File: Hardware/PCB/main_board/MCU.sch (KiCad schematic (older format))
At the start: 2 parts, among them J1 SWD, U2 NUCLEO-F446RE

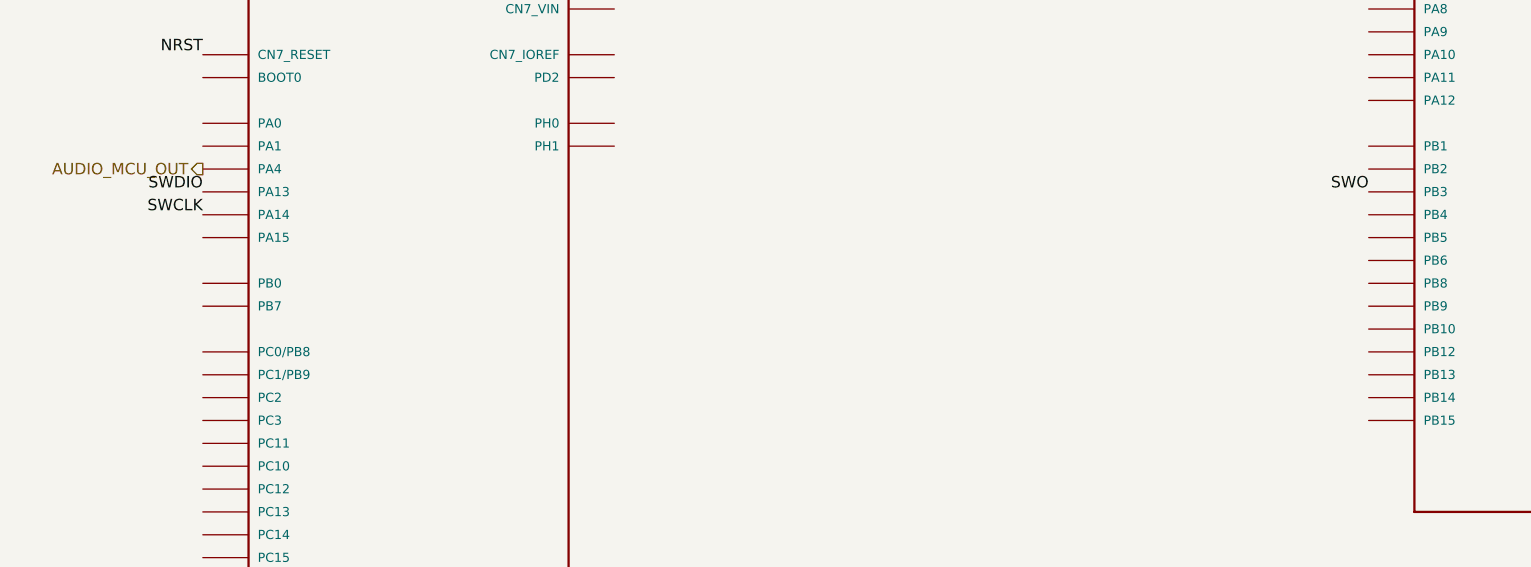
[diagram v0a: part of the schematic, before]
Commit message: Place VCF components, I2C bus
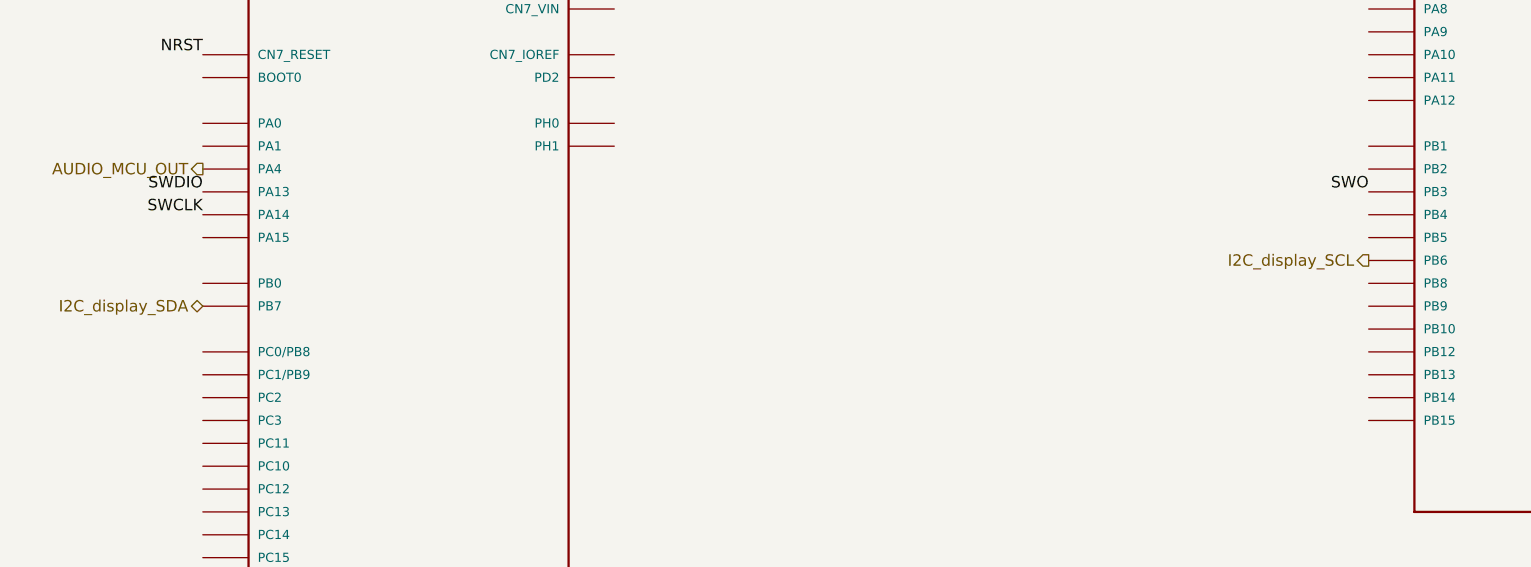
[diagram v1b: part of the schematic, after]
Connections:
- net I2C_display_SDA: now reaches U2.CN7_21 (PB7)
- net I2C_display_SCL: now reaches U2.CN10_17 (PB6)
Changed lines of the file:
@@
 $Descr A4 11693 8268
 encoding utf-8
-Sheet 3 7
+Sheet 7 7
 Title ""
 Date ""
@@
 Text Notes 4600 2050 0    50   Italic 0
 +3.3V is sourced from\nthe Nucleo board
+Text HLabel 7650 3650 0    50   Output ~ 0
+I2C_display_SCL
+Text HLabel 2550 3850 0    50   BiDi ~ 0
+I2C_display_SDA
 $EndSCHEMATC

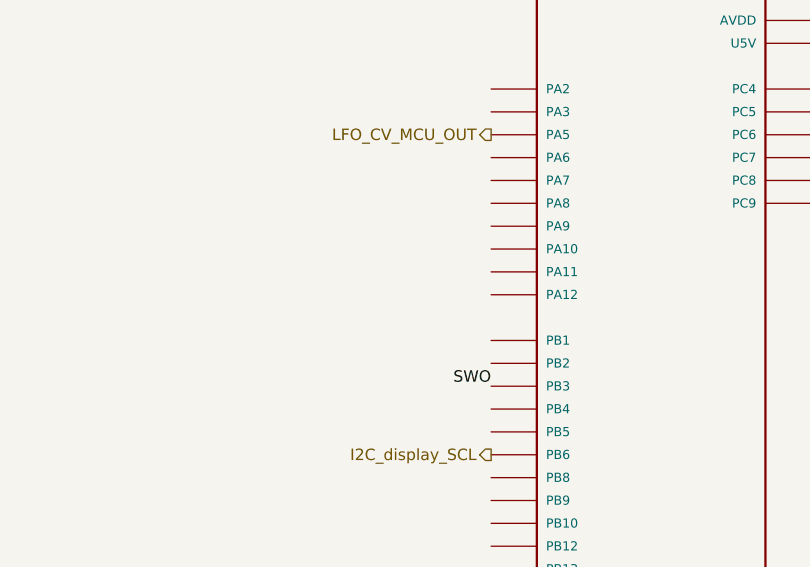
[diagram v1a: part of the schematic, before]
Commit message: Update 3D view
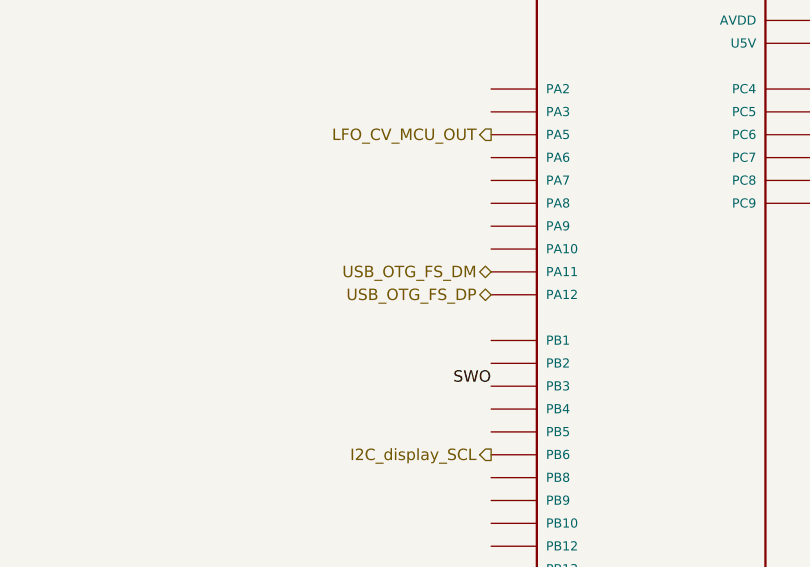
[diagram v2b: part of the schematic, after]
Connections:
- net USB_OTG_FS_DP: now reaches U2.CN10_12 (PA12)
- net USB_OTG_FS_DM: now reaches U2.CN10_14 (PA11)
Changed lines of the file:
@@
 Text HLabel 2550 3850 0    50   BiDi ~ 0
 I2C_display_SDA
+Text HLabel 7650 2950 0    50   BiDi ~ 0
+USB_OTG_FS_DP
+Text HLabel 7650 2850 0    50   BiDi ~ 0
+USB_OTG_FS_DM
 $EndSCHEMATC

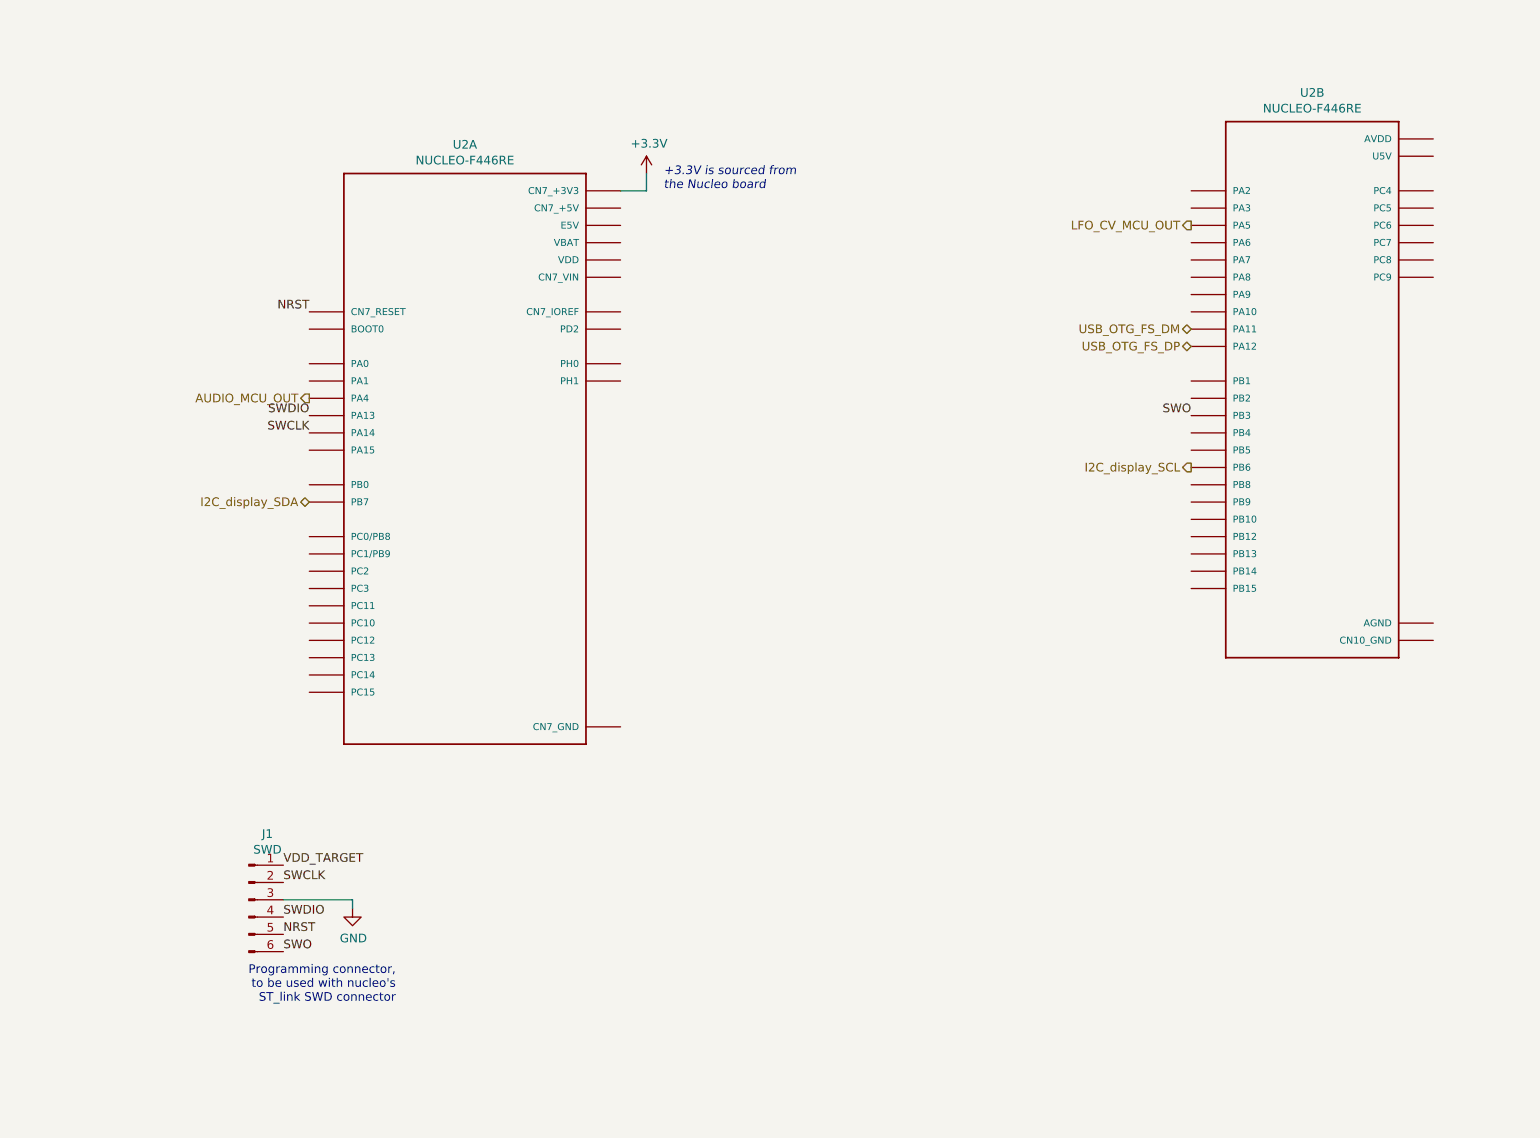
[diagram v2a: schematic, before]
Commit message: Route GPIO
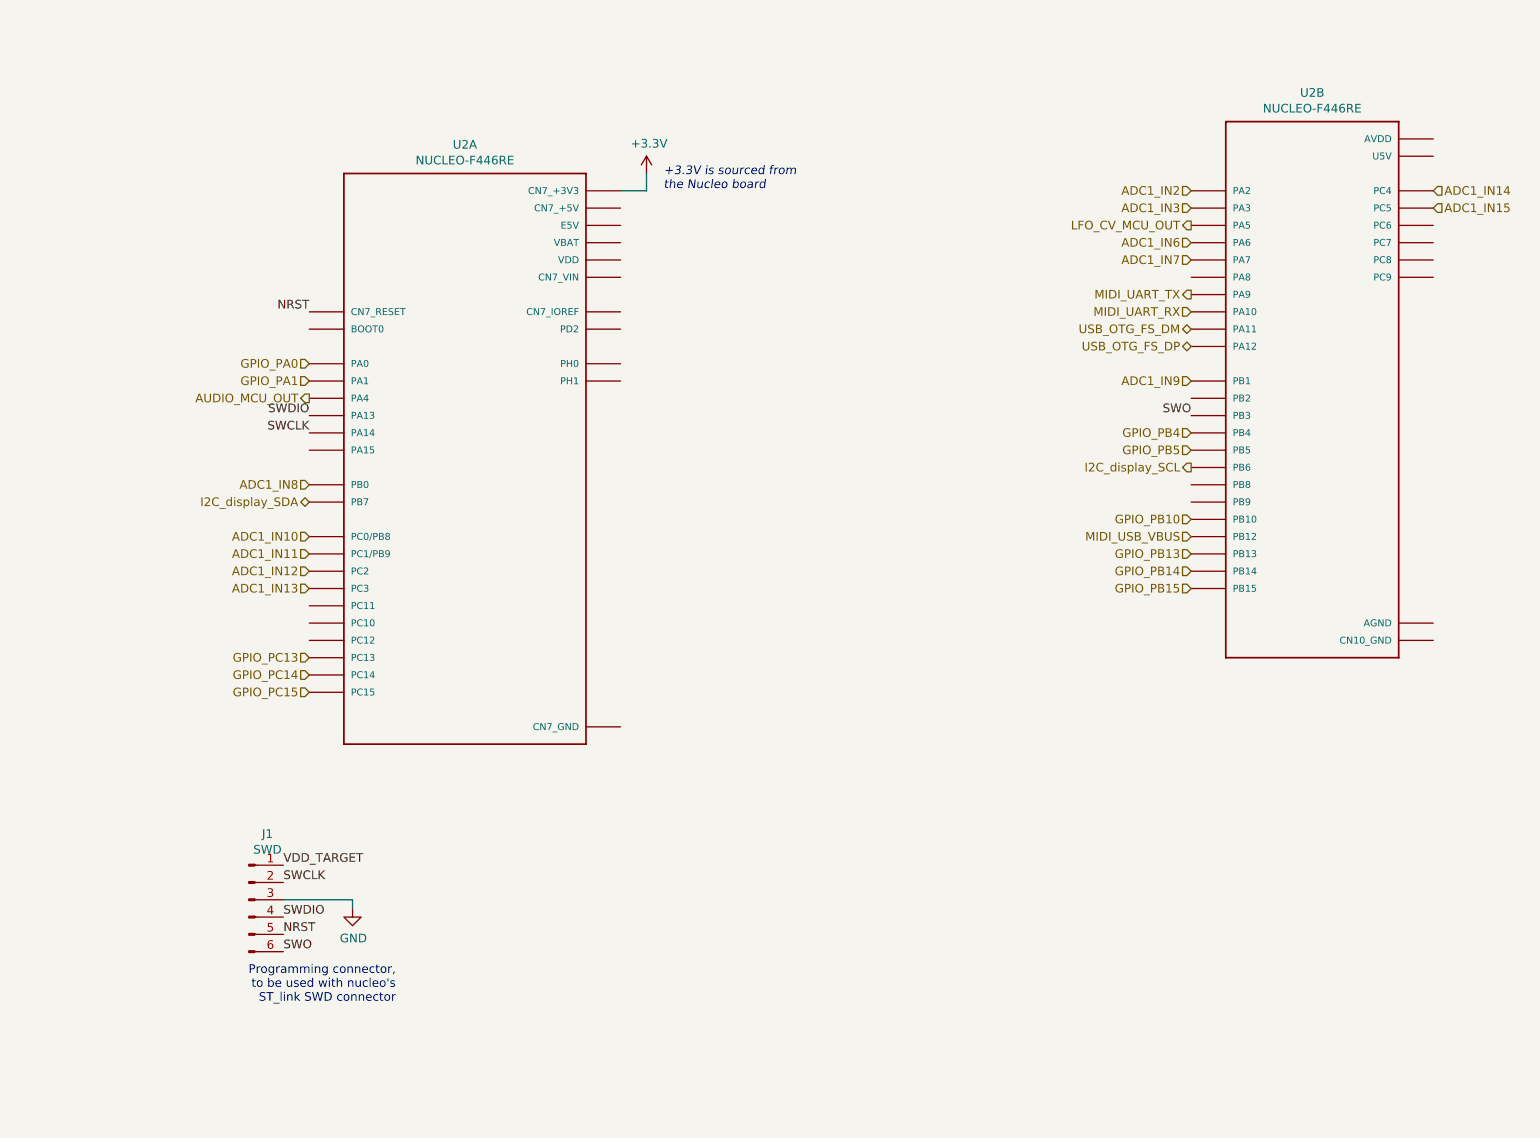
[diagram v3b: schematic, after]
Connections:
- net GPIO_PC13: now reaches U2.CN7_23 (PC13)
- net GPIO_PC14: now reaches U2.CN7_25 (PC14)
- net GPIO_PC15: now reaches U2.CN7_27 (PC15)
- net GPIO_PA0: now reaches U2.CN7_28 (PA0)
- net GPIO_PA1: now reaches U2.CN7_30 (PA1)
- net ADC1_IN8: now reaches U2.CN7_34 (PB0)
- net ADC1_IN12: now reaches U2.CN7_35 (PC2)
- net ADC1_IN11: now reaches U2.CN7_36 (PC1/PB9)
- net ADC1_IN13: now reaches U2.CN7_37 (PC3)
- net ADC1_IN10: now reaches U2.CN7_38 (PC0/PB8)
- net ADC1_IN6: now reaches U2.CN10_13 (PA6)
- net ADC1_IN7: now reaches U2.CN10_15 (PA7)
- net MIDI_USB_VBUS: now reaches U2.CN10_16 (PB12)
- net MIDI_UART_TX: now reaches U2.CN10_21 (PA9)
- net ADC1_IN9: now reaches U2.CN10_24 (PB1)
- net GPIO_PB10: now reaches U2.CN10_25 (PB10)
- net GPIO_PB15: now reaches U2.CN10_26 (PB15)
- net GPIO_PB4: now reaches U2.CN10_27 (PB4)
- net GPIO_PB14: now reaches U2.CN10_28 (PB14)
- net GPIO_PB5: now reaches U2.CN10_29 (PB5)
- net GPIO_PB13: now reaches U2.CN10_30 (PB13)
- net MIDI_UART_RX: now reaches U2.CN10_33 (PA10)
- net ADC1_IN14: now reaches U2.CN10_34 (PC4)
- net ADC1_IN2: now reaches U2.CN10_35 (PA2)
- net ADC1_IN3: now reaches U2.CN10_37 (PA3)
- net ADC1_IN15: now reaches U2.CN10_6 (PC5)
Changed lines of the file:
@@
 Text HLabel 7650 2850 0    50   BiDi ~ 0
 USB_OTG_FS_DM
+Text HLabel 7650 2650 0    50   Output ~ 0
+MIDI_UART_TX
+Text HLabel 7650 2750 0    50   Input ~ 0
+MIDI_UART_RX
+Text HLabel 7650 4050 0    50   Input ~ 0
+MIDI_USB_VBUS
+Text HLabel 2550 4050 0    50   Input ~ 0
+ADC1_IN10
+Text HLabel 2550 4150 0    50   Input ~ 0
+ADC1_IN11
+Text HLabel 2550 4250 0    50   Input ~ 0
+ADC1_IN12
+Text HLabel 2550 4350 0    50   Input ~ 0
+ADC1_IN13
+Text HLabel 7650 2050 0    50   Input ~ 0
+ADC1_IN2
+Text HLabel 7650 2150 0    50   Input ~ 0
+ADC1_IN3
+Text HLabel 7650 2350 0    50   Input ~ 0
+ADC1_IN6
+Text HLabel 7650 2450 0    50   Input ~ 0
+ADC1_IN7
+Text HLabel 9050 2050 2    50   Input ~ 0
+ADC1_IN14
+Text HLabel 9050 2150 2    50   Input ~ 0
+ADC1_IN15
+Text HLabel 7650 3150 0    50   Input ~ 0
+ADC1_IN9
+Text HLabel 2550 3750 0    50   Input ~ 0
+ADC1_IN8
+Text HLabel 2550 3050 0    50   Input ~ 0
+GPIO_PA0
+Text HLabel 2550 3150 0    50   Input ~ 0
+GPIO_PA1
+Text HLabel 2550 4750 0    50   Input ~ 0
+GPIO_PC13
+Text HLabel 2550 4850 0    50   Input ~ 0
+GPIO_PC14
+Text HLabel 2550 4950 0    50   Input ~ 0
+GPIO_PC15
+Text HLabel 7650 4150 0    50   Input ~ 0
+GPIO_PB13
+Text HLabel 7650 4250 0    50   Input ~ 0
+GPIO_PB14
+Text HLabel 7650 4350 0    50   Input ~ 0
+GPIO_PB15
+Text HLabel 7650 3450 0    50   Input ~ 0
+GPIO_PB4
+Text HLabel 7650 3550 0    50   Input ~ 0
+GPIO_PB5
+Text HLabel 7650 3950 0    50   Input ~ 0
+GPIO_PB10
 $EndSCHEMATC

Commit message: Route PWR
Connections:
- net GND: now also U2.CN10_20 (CN10_GND), U2.CN10_32 (AGND), U2.CN10_9 (CN10_GND), U2.CN7_19 (CN7_GND), U2.CN7_20 (CN7_GND), U2.CN7_22 (CN7_GND), U2.CN7_8 (CN7_GND)
- net +5V: now reaches U2.CN7_6 (E5V)
- no-connect marks 0 -> 23
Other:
- note added: "+3.3V power output\n(+3.3V is sourced from\nthe Nucleo board)"
- note added: "nucleo power input"
- note removed: "+3.3V is sourced from\nthe Nucleo board"
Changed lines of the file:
@@
 Wire Wire Line
 	4500 2050 4500 1950
-Text Notes 4600 2050 0    50   Italic 0
-+3.3V is sourced from\nthe Nucleo board
+Text Notes 4650 1850 0    50   Italic 0
++3.3V power output\n(+3.3V is sourced from\nthe Nucleo board)
 Text HLabel 7650 3650 0    50   Output ~ 0
 I2C_display_SCL
@@
 Text HLabel 7650 3950 0    50   Input ~ 0
 GPIO_PB10
+Wire Wire Line
+	9050 4550 9150 4550
+Wire Wire Line
+	9150 4550 9150 4650
+Wire Wire Line
+	9150 4650 9050 4650
+Wire Wire Line
+	9150 4650 9150 4700
+Connection ~ 9150 4650
+$Comp
+L power:GND #PWR0121
+U 1 1 5E925AA7
+P 9150 4700
+F 0 "#PWR0121" H 9150 4450 50  0001 C CNN
+F 1 "GND" H 9155 4527 50  0000 C CNN
+F 2 "" H 9150 4700 50  0001 C CNN
+F 3 "" H 9150 4700 50  0001 C CNN
+	1    9150 4700
+	1    0    0    -1
+$EndComp
+Wire Wire Line
+	4350 5150 4450 5150
+Wire Wire Line
+	4450 5150 4450 5250
+$Comp
+L power:GND #PWR0122
+U 1 1 5E9284C5
+P 4450 5250
+F 0 "#PWR0122" H 4450 5000 50  0001 C CNN
+F 1 "GND" H 4455 5077 50  0000 C CNN
+F 2 "" H 4450 5250 50  0001 C CNN
+F 3 "" H 4450 5250 50  0001 C CNN
+	1    4450 5250
+	1    0    0    -1
+$EndComp
+NoConn ~ 2550 2850
+NoConn ~ 2550 3550
+NoConn ~ 2550 4450
+NoConn ~ 2550 4550
+NoConn ~ 2550 4650
+NoConn ~ 4350 3150
+NoConn ~ 4350 3050
+NoConn ~ 4350 2850
+NoConn ~ 4350 2750
+NoConn ~ 4350 2550
+NoConn ~ 4350 2350
+NoConn ~ 4350 2450
+NoConn ~ 4350 2150
+NoConn ~ 7650 2550
+NoConn ~ 7650 3250
+NoConn ~ 7650 3750
+NoConn ~ 7650 3850
+NoConn ~ 9050 1750
+NoConn ~ 9050 1850
+NoConn ~ 9050 2250
+NoConn ~ 9050 2350
+NoConn ~ 9050 2450
+NoConn ~ 9050 2550
+Wire Wire Line
+	4350 2250 4750 2250
+Wire Wire Line
+	4750 2250 4750 2200
+$Comp
+L power:+5V #PWR?
+U 1 1 5E9D24A0
+P 4750 2200
+F 0 "#PWR?" H 4750 2050 50  0001 C CNN
+F 1 "+5V" H 4765 2373 50  0000 C CNN
+F 2 "" H 4750 2200 50  0001 C CNN
+F 3 "" H 4750 2200 50  0001 C CNN
+	1    4750 2200
+	1    0    0    -1
+$EndComp
+Text Notes 4850 2200 0    50   Italic 0
+nucleo power input
 $EndSCHEMATC

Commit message: Change GPIO config
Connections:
- net GPIO_PB8: now reaches U2.CN10_3 (PB8)
- net GPIO_PB9: now reaches U2.CN10_5 (PB9)
- net GPIO_PB14 renamed USB_DEV_HS_DM
- net GPIO_PB15 renamed USB_DEV_HS_DP
- no-connect marks 23 -> 21
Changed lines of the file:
@@
 encoding utf-8
 Sheet 7 7
-Title ""
-Date ""
-Rev ""
-Comp ""
-Comment1 ""
+Title "MiniMood"
+Date "2020"
+Rev "A"
+Comp "INSA Rennes"
+Comment1 "Heol Fief, Vincent Colombel, Julien le Pelve, Loïc Scotto"
 Comment2 ""
 Comment3 ""
@@
 Text HLabel 7650 4150 0    50   Input ~ 0
 GPIO_PB13
-Text HLabel 7650 4250 0    50   Input ~ 0
-GPIO_PB14
-Text HLabel 7650 4350 0    50   Input ~ 0
-GPIO_PB15
+Text HLabel 7650 3750 0    50   Input ~ 0
+GPIO_PB8
+Text HLabel 7650 3850 0    50   Input ~ 0
+GPIO_PB9
 Text HLabel 7650 3450 0    50   Input ~ 0
 GPIO_PB4
@@
 NoConn ~ 7650 2550
 NoConn ~ 7650 3250
-NoConn ~ 7650 3750
-NoConn ~ 7650 3850
 NoConn ~ 9050 1750
 NoConn ~ 9050 1850
@@
 	4750 2250 4750 2200
 $Comp
-L power:+5V #PWR?
+L power:+5V #PWR0123
 U 1 1 5E9D24A0
 P 4750 2200
-F 0 "#PWR?" H 4750 2050 50  0001 C CNN
+F 0 "#PWR0123" H 4750 2050 50  0001 C CNN
 F 1 "+5V" H 4765 2373 50  0000 C CNN
 F 2 "" H 4750 2200 50  0001 C CNN
@@
 Text Notes 4850 2200 0    50   Italic 0
 nucleo power input
+Text HLabel 7650 4250 0    50   BiDi ~ 0
+USB_DEV_HS_DM
+Text HLabel 7650 4350 0    50   BiDi ~ 0
+USB_DEV_HS_DP
 $EndSCHEMATC

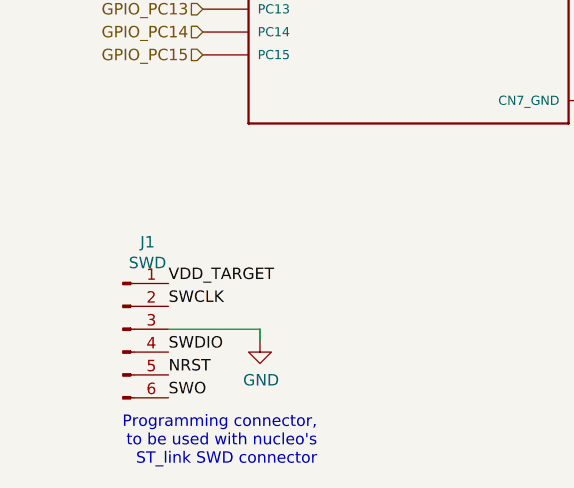
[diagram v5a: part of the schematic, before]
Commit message: Add FX buffer and headphone amp to schematics
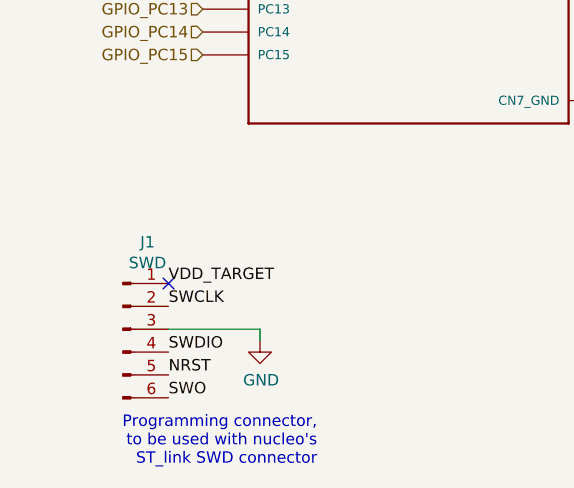
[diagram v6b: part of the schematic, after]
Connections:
- no-connect marks 21 -> 22
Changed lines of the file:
@@
 Text HLabel 7650 4350 0    50   BiDi ~ 0
 USB_DEV_HS_DP
+NoConn ~ 2400 5950
 $EndSCHEMATC
